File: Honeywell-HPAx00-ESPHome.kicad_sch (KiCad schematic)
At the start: 27 parts, among them J1 Conn_01x06, J2 Conn_01x01, J3 Conn_01x01, J4 Conn_01x01, J5 Conn_01x01, J6 Conn_01x01, J7 Conn_01x01, J8 Conn_01x02, U1 mini_esp32

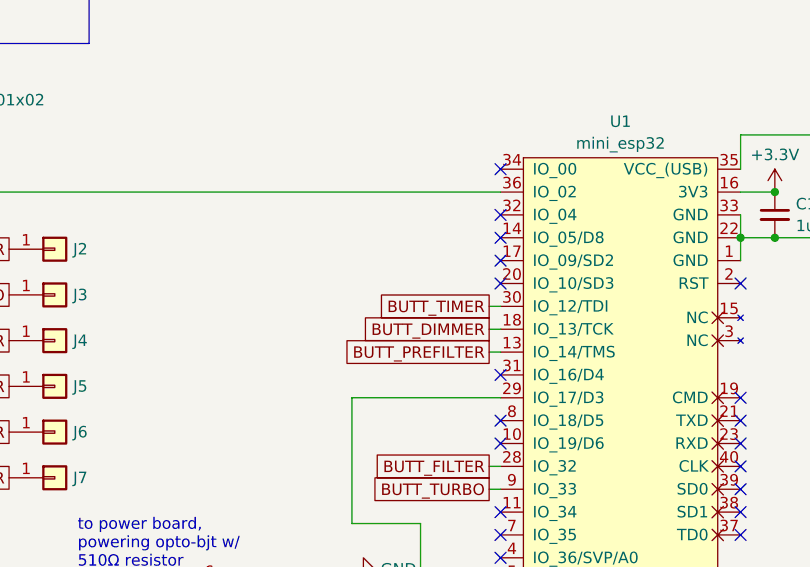
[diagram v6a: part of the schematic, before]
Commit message: Move prefilter to GPIO4 (#1)
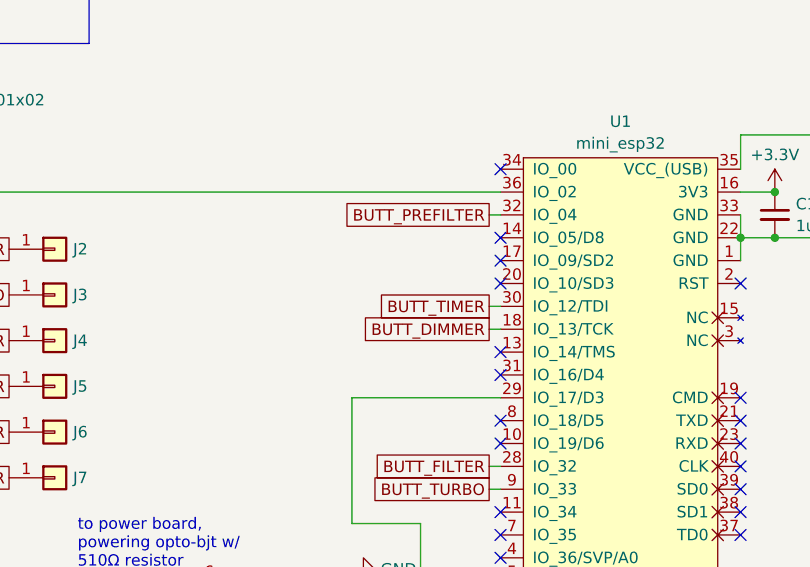
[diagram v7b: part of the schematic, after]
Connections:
- net BUTT_PREFILTER: now also U1.32 (IO_04); no longer U1.13 (IO_14/TMS)
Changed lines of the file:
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@@
+	)
+	(no_connect
+		(at 146.05 73.66)
 	)
 	(no_connect
@@
 	)
 	(no_connect
-		(at 146.05 58.42)
-	)
-	(no_connect
 		(at 146.05 76.2)
 	)
@@
 	(wire
 		(pts
-			(xy 144.78 73.66) (xy 146.05 73.66)
-		)
-		(stroke
-			(width 0)
-			(type default)
-		)
-	)
-	(wire
-		(pts
 			(xy 168.91 129.54) (xy 184.15 129.54)
 		)
@@
 		(pts
 			(xy 129.54 92.71) (xy 137.16 92.71)
+		)
+		(stroke
+			(width 0)
+			(type default)
+		)
+	)
+	(wire
+		(pts
+			(xy 144.78 58.42) (xy 146.05 58.42)
 		)
 		(stroke
@@
 	(global_label "BUTT_PREFILTER"
 		(shape passive)
-		(at 144.78 73.66 180)
+		(at 144.78 58.42 180)
 		(fields_autoplaced yes)
 		(effects
@@
 		)
 		(property "Intersheetrefs" "${INTERSHEET_REFS}"
-			(at 128.5733 73.66 0)
+			(at 128.5733 58.42 0)
 			(effects
 				(font

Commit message: Updated PCB with new spring footprints
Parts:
- J2, J3, J4, J5, J6, J7: footprint TestPoint:TestPoint_THTPad_D2.0mm_Drill1.0mm -> TestPoint:Honeywell V1+2 Spring
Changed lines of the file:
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@@
 			)
 		)
-		(property "Footprint" "TestPoint:TestPoint_THTPad_D2.0mm_Drill1.0mm"
+		(property "Footprint" "TestPoint:Honeywell V1+2 Spring"
 			(at 96.52 82.55 0)
 			(effects
@@
 			)
 		)
-		(property "Footprint" "TestPoint:TestPoint_THTPad_D2.0mm_Drill1.0mm"
+		(property "Footprint" "TestPoint:Honeywell V1+2 Spring"
 			(at 96.52 87.63 0)
 			(effects
@@
 			)
 		)
-		(property "Footprint" "TestPoint:TestPoint_THTPad_D2.0mm_Drill1.0mm"
+		(property "Footprint" "TestPoint:Honeywell V1+2 Spring"
 			(at 96.52 62.23 0)
 			(effects
@@
 			)
 		)
-		(property "Footprint" "TestPoint:TestPoint_THTPad_D2.0mm_Drill1.0mm"
+		(property "Footprint" "TestPoint:Honeywell V1+2 Spring"
 			(at 96.52 77.47 0)
 			(effects
@@
 			)
 		)
-		(property "Footprint" "TestPoint:TestPoint_THTPad_D2.0mm_Drill1.0mm"
+		(property "Footprint" "TestPoint:Honeywell V1+2 Spring"
 			(at 96.52 72.39 0)
 			(effects
@@
 			)
 		)
-		(property "Footprint" "TestPoint:TestPoint_THTPad_D2.0mm_Drill1.0mm"
+		(property "Footprint" "TestPoint:Honeywell V1+2 Spring"
 			(at 96.52 67.31 0)
 			(effects
